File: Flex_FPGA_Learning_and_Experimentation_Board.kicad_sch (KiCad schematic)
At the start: 1 part, among them U1 XC7A35T-FTG256

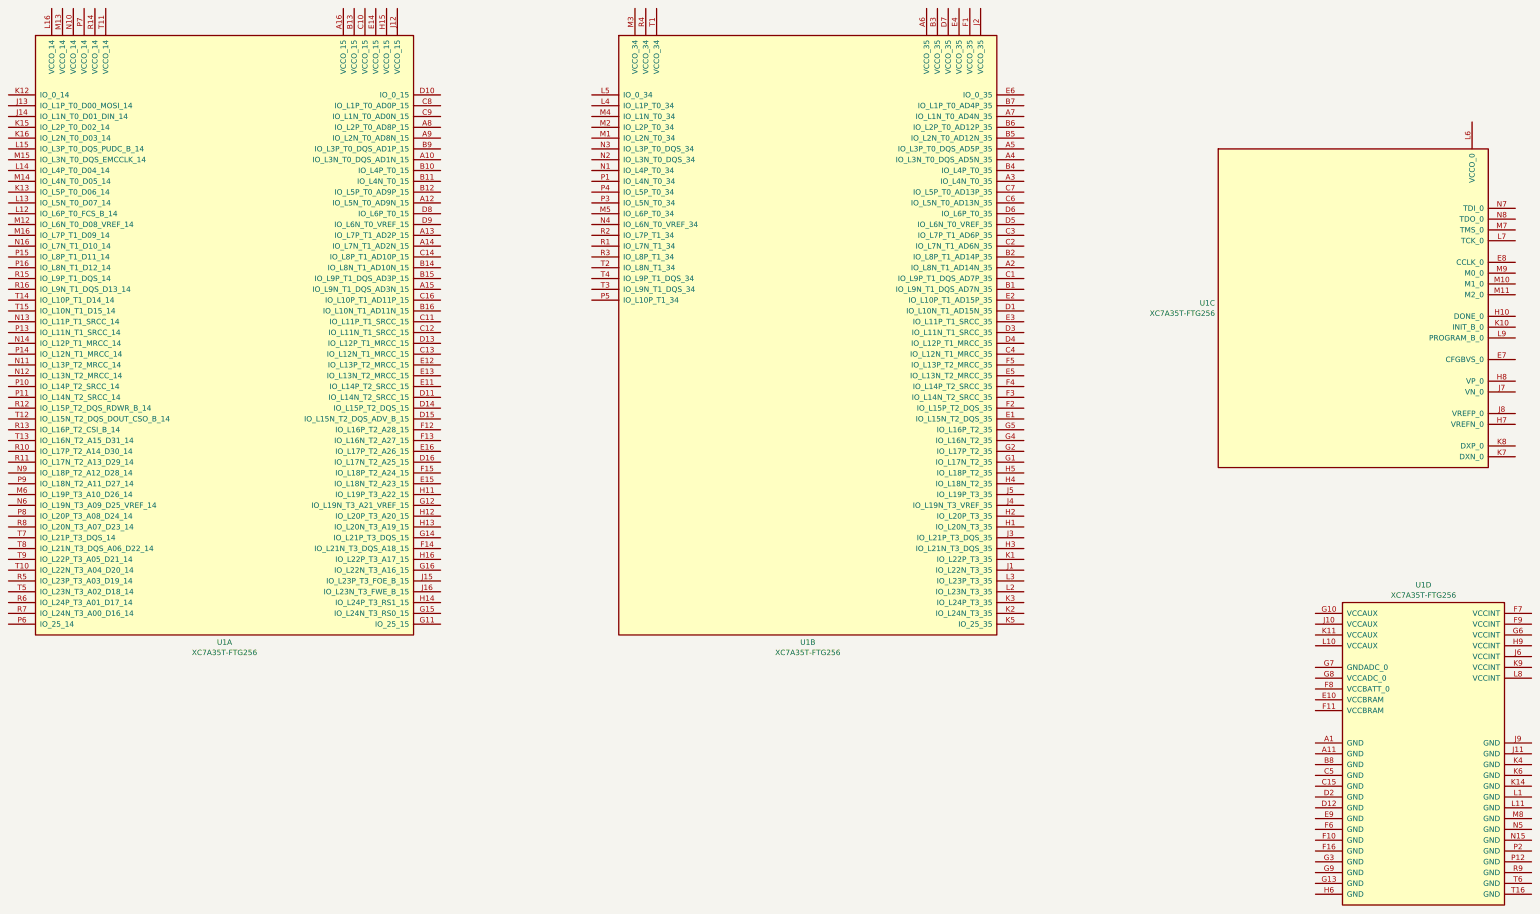
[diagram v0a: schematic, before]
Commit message: update schematic
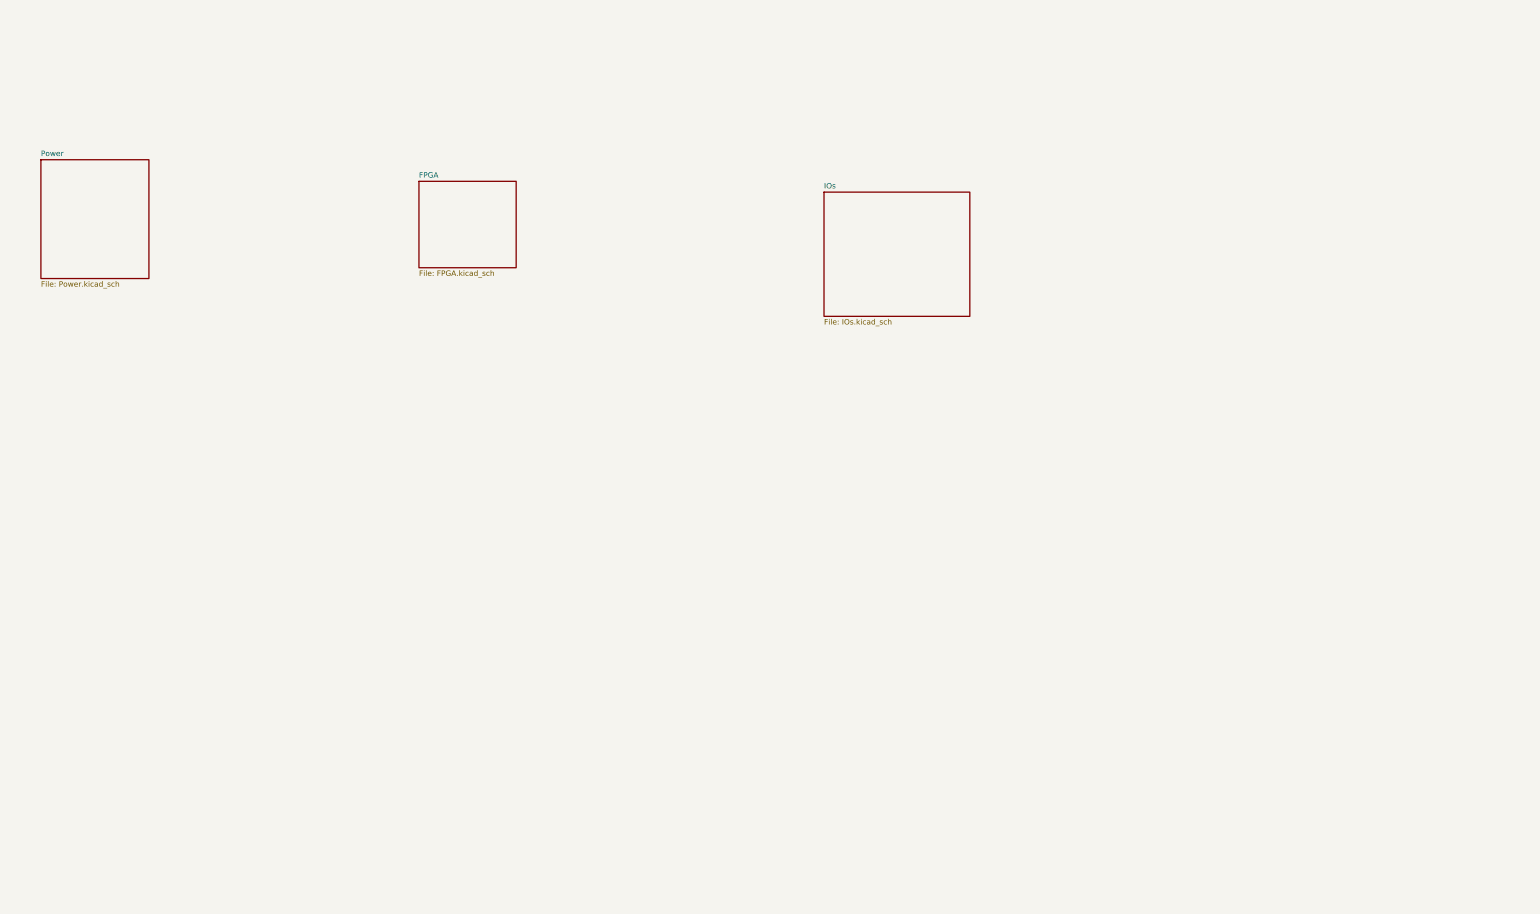
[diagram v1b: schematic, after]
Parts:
- removed U1: XC7A35T-FTG256, symbol FPGA_Xilinx_Artix7:XC7A35T-FTG256
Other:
- added sheet FPGA (FPGA.kicad_sch)
- added sheet IOs (IOs.kicad_sch)
- added sheet Power (Power.kicad_sch)
